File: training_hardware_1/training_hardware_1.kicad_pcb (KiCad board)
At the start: 2 copper layers, 96.5 x 43.2 mm, 17 parts, among them J1 RJ45_LED_Shielded, U1 Teensy4.1_DEV-16771, U2 OKI, U3 ATA6561-GAQW-N

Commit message: Add wire length
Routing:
- net /MCU/LED: track 0.00 -> 79.7 mm
- net /CAN/STBY: track 0.00 -> 44.1 mm, vias 0 -> 1
- net /MCU/Rx-: track 57.5 -> 65.0 mm
- net +3V3: track 37.2 -> 39.9 mm
- net /MCU/Tx+: track 67.3 -> 68.0 mm

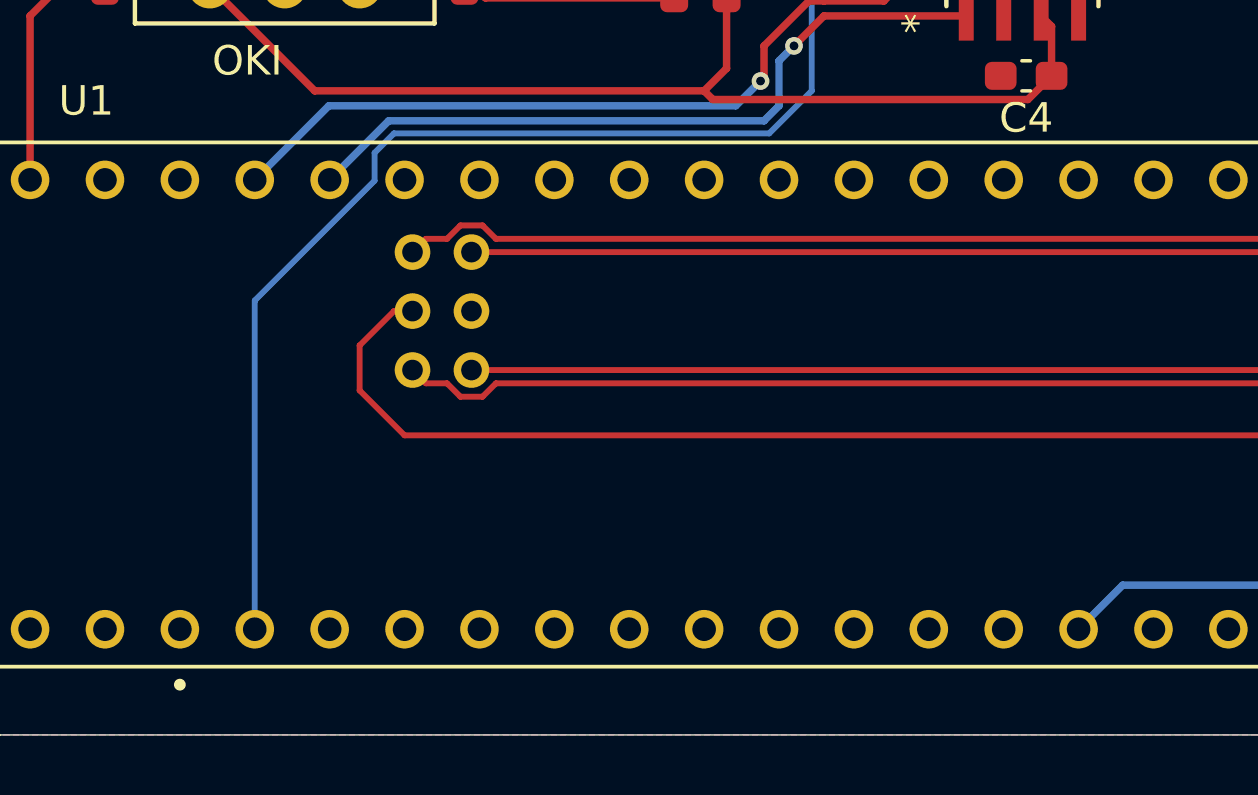
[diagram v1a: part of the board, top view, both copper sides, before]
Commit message: Add 3v3 wire
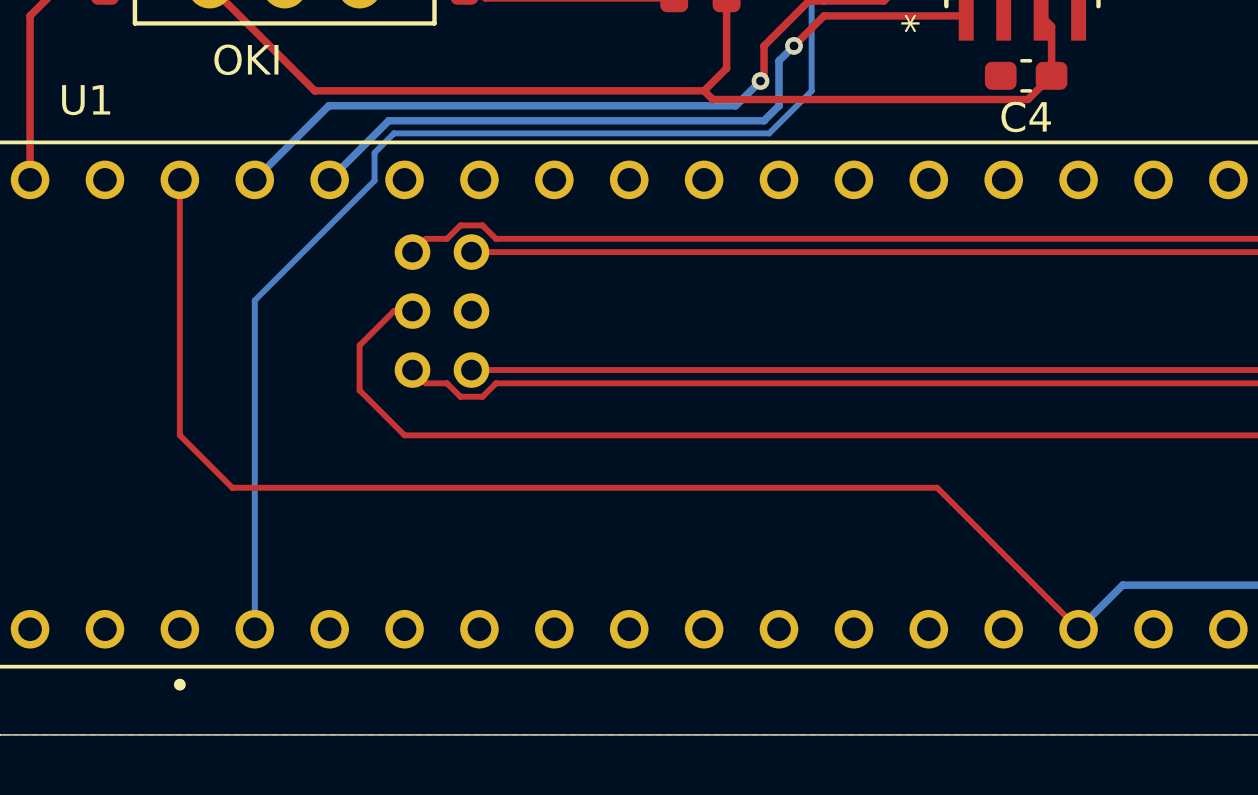
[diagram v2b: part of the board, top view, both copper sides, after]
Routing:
- net +3V3: track 39.9 -> 81.8 mm
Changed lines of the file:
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@@
+	)
+	(segment
+		(start 134.62 67.5357)
+		(end 134.62 76.2)
+		(width 0.2)
+		(layer "F.Cu")
+		(net 5)
 	)
 	(segment
@@
 		(layer "F.Cu")
 		(net 5)
+	)
+	(segment
+		(start 160.3023 77.978)
+		(end 165.1 82.7757)
+		(width 0.2)
+		(layer "F.Cu")
+		(net 5)
+	)
+	(segment
+		(start 136.398 77.978)
+		(end 160.3023 77.978)
+		(width 0.2)
+		(layer "F.Cu")
+		(net 5)
+	)
+	(segment
+		(start 134.62 76.2)
+		(end 136.398 77.978)
+		(width 0.2)
+		(layer "F.Cu")
+		(net 5)
